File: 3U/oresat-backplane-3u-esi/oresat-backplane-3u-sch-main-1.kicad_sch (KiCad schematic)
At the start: 28 parts

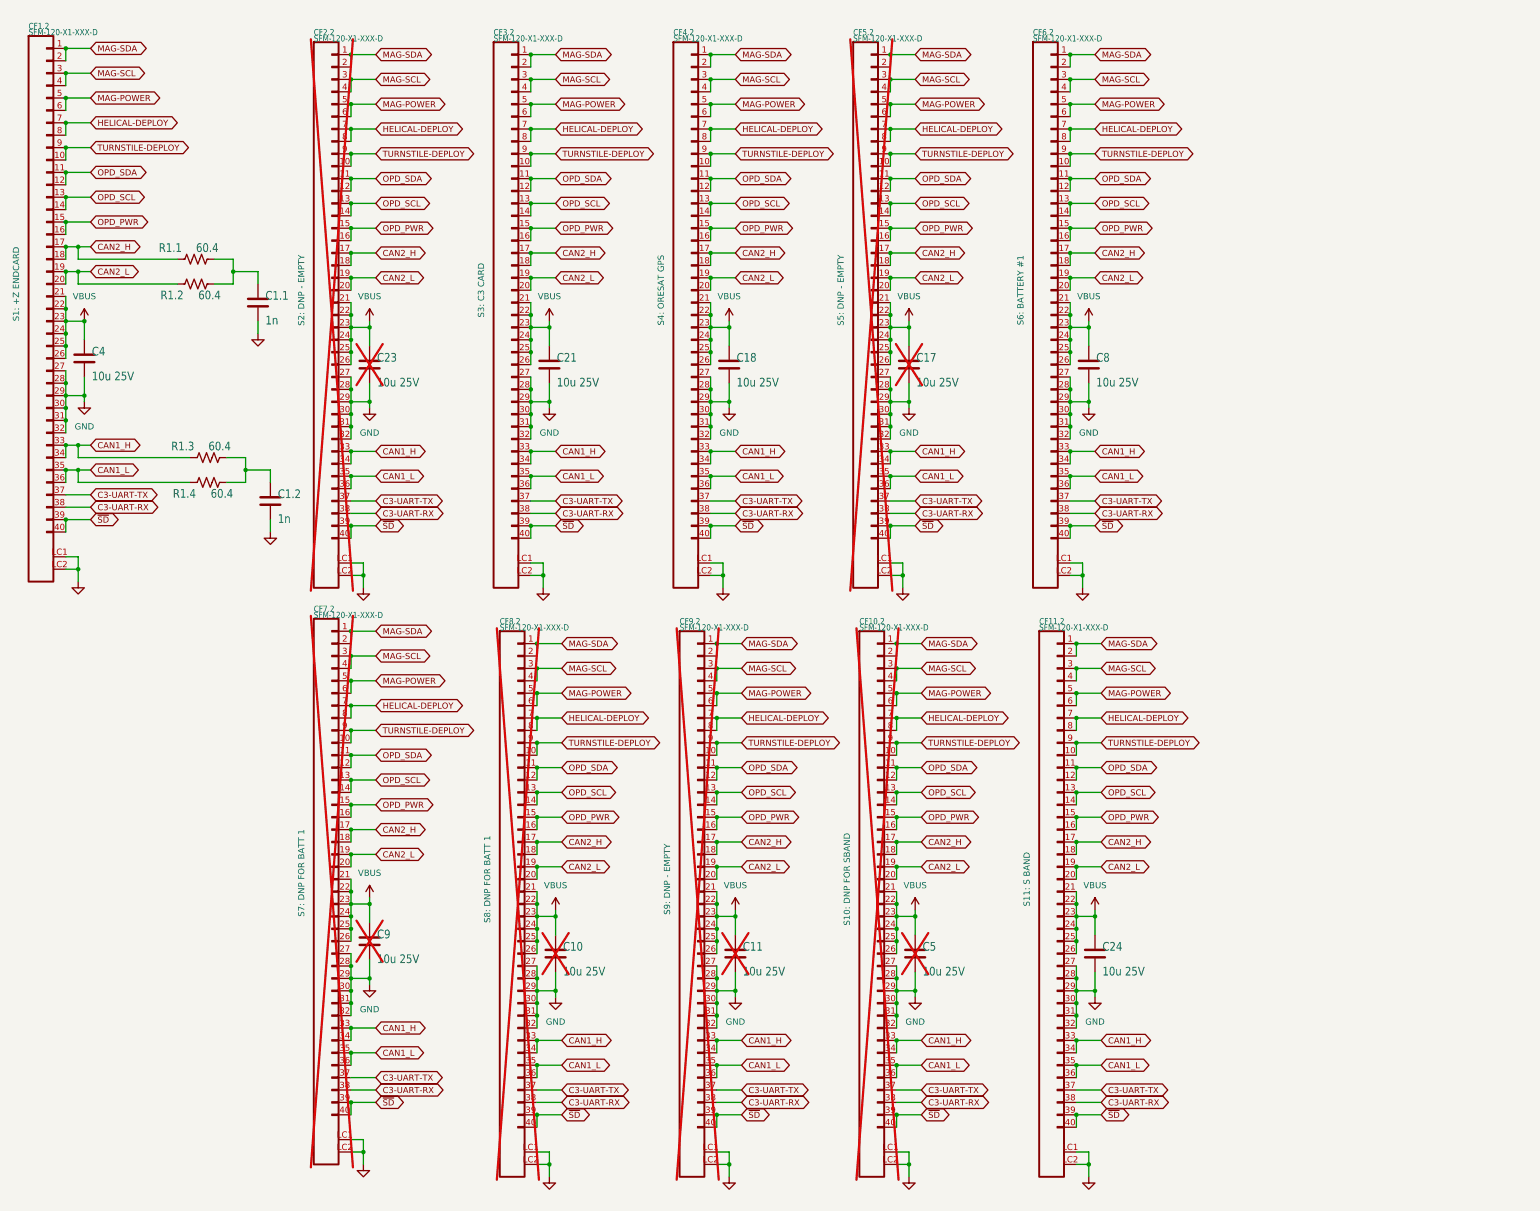
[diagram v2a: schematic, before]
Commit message: Polish of 3U for ESI
Fixed ERC/DRC/sync errors. Made fancy RF table. Fixed BOM.
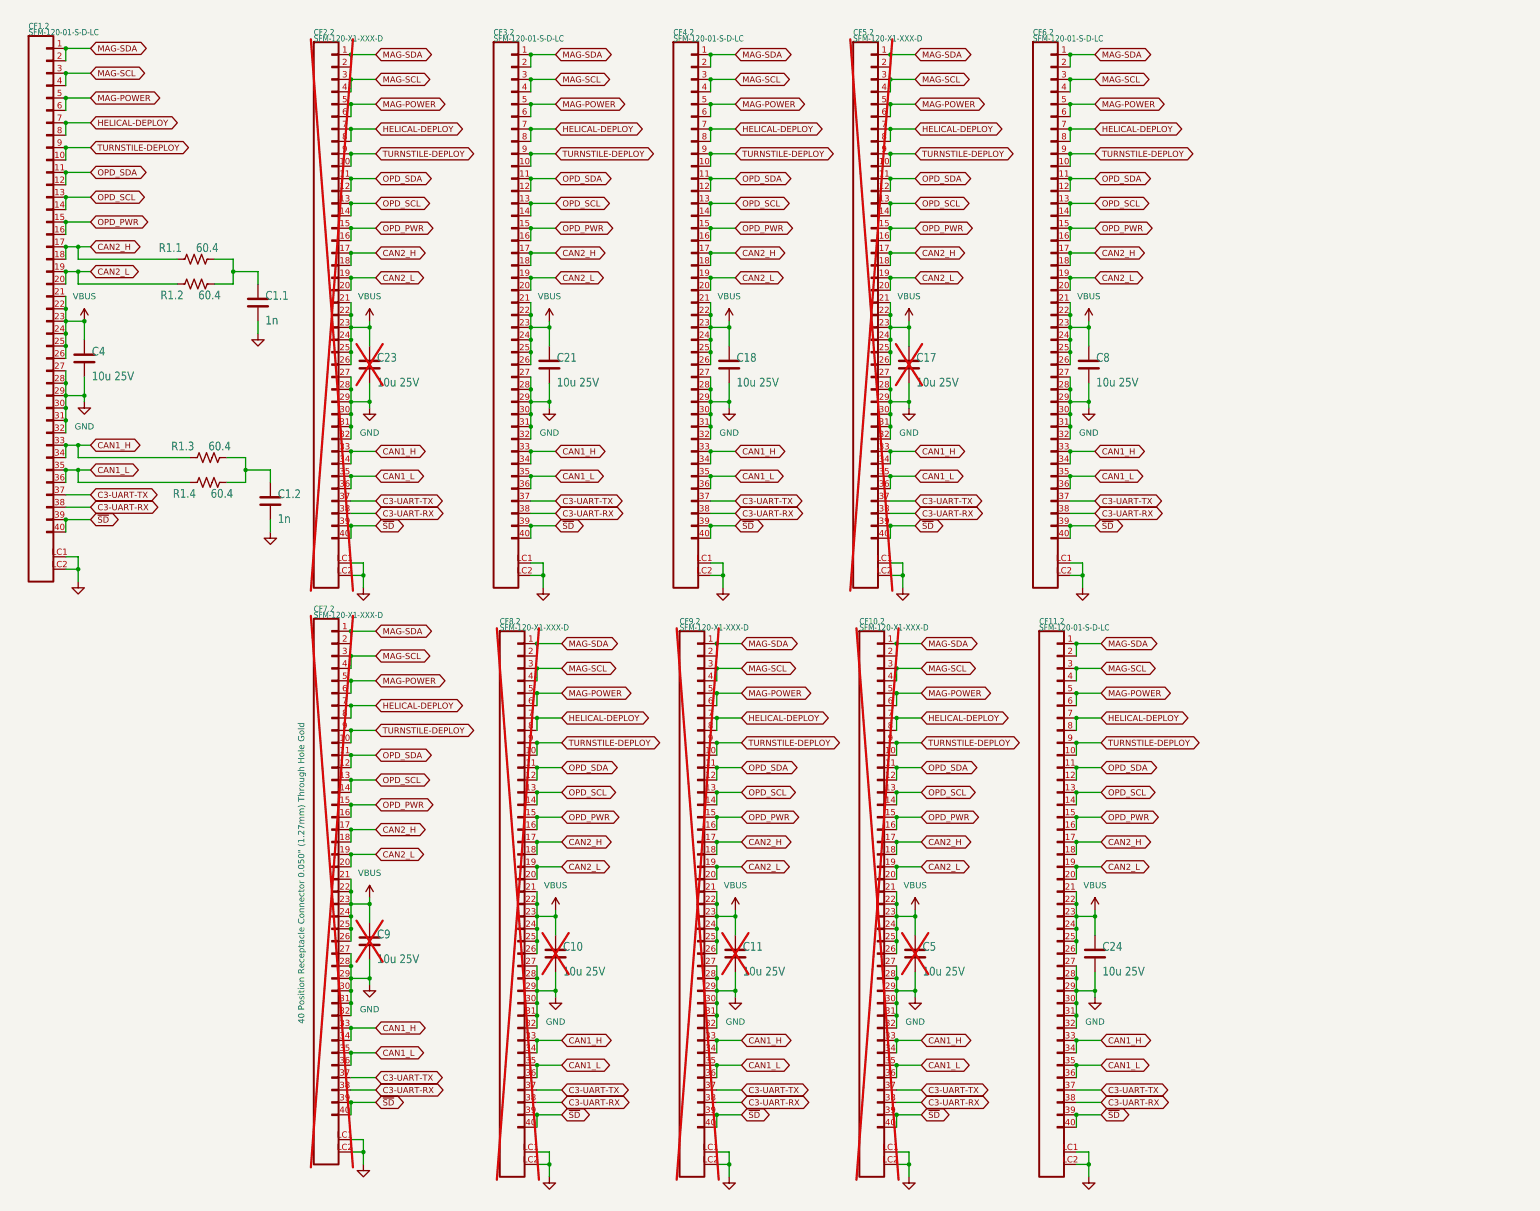
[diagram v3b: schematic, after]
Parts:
- C1.1, C1.2: DIS (none) -> DigiKey; DPN (none) -> 399-C0603C102J5GECAUTOCT-ND; MFR (none) -> KEMET; MPN (none) -> C0603C102J5GECAUTO
- C10, C11, C17, C18, C21, C23, C24, C4, C5, C8, C9: DIS (none) -> DigiKey; DPN (none) -> 587-3485-1-ND; MFR (none) -> Taiyo Yuden; MPN (none) -> TMK316AB7106KLHT
- CF1.2, CF11.2, CF3.2, CF4.2, CF6.2: value SFM-120-X1-XXX-D -> SFM-120-01-S-D-LC; DIS (none) -> DigiKey; DPN (none) -> SAM11706-ND; MFR (none) -> Samtec Inc.; MPN (none) -> SFM-120-01-S-D-LC
- CF10.2, CF2.2, CF5.2, CF7.2, CF8.2, CF9.2: DIS (none) -> DigiKey; DPN (none) -> SAM11706-ND; MFR (none) -> Samtec Inc.; MPN (none) -> SFM-120-01-S-D-LC
- R1.1, R1.2, R1.3, R1.4: DIS (none) -> DigiKey; DPN (none) -> RMCF1206FT60R4CT-ND; MFR (none) -> Stackpole Electronics Inc; MPN (none) -> RMCF1206FT60R4
